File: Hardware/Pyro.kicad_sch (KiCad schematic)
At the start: 60 parts, among them J12 Conn_01x02_Male, J14 Conn_01x02_Male, J15 Conn_01x02_Male, Q7 BSZ025N04LS, Q8 BSZ025N04LS, Q9 BSZ025N04LS, U10 SiC438BED-T1-GE3, U11 782-TCMT1109, U12 INA219AxDCN, U15 782-TCMT1109, U9 782-TCMT1109

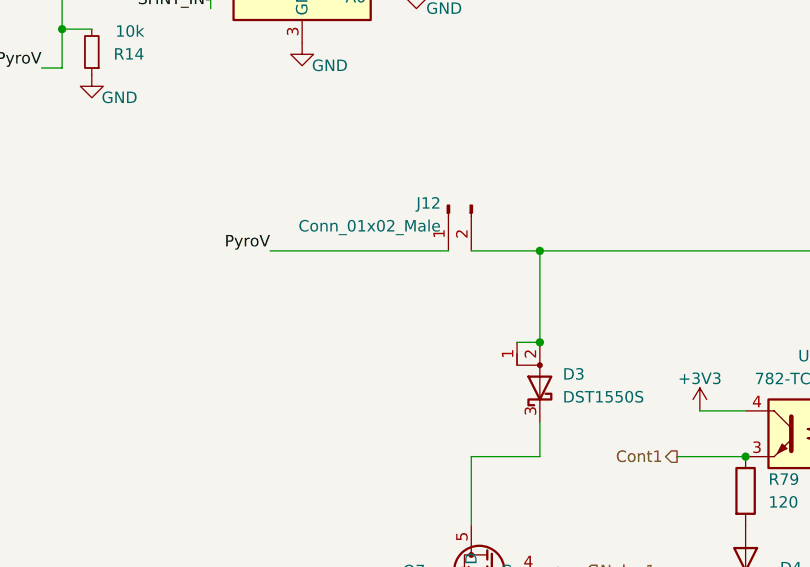
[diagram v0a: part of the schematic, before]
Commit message: Added flyback on pyro channel
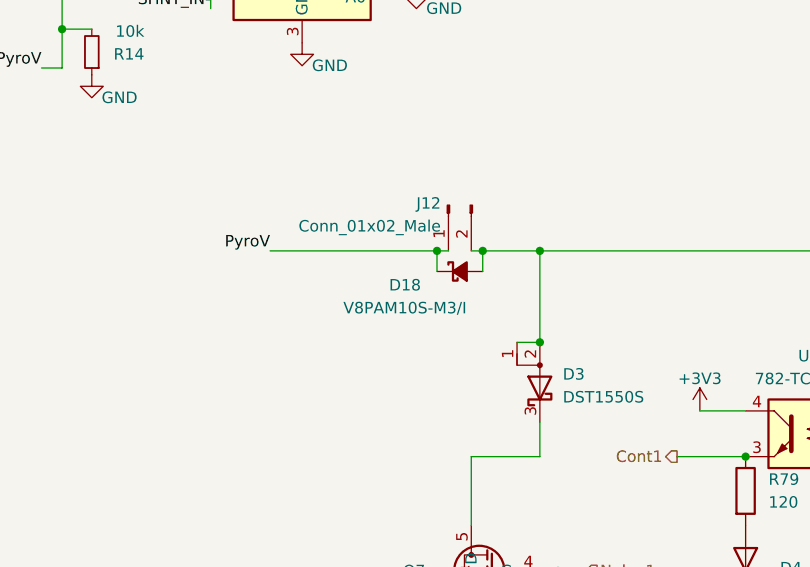
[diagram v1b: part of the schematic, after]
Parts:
- added D18: V8PAM10S-M3/I, iclr:V8PAM10SM3I, symbol Device:D_Schottky_Small_Filled
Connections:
- net PyroV: now also D18.1 (K)
- net at D3.1 (A), D3.2 (A), J12.2 (Pin_2)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: now also D18.2 (A)
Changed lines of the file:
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@@
 	)
 	(junction
+		(at 206.756 72.136)
+		(diameter 0)
+		(color 0 0 0 0)
+	)
+	(junction
 		(at 87.63 103.378)
 		(diameter 0)
@@
 		(color 0 0 0 0)
 	)
+	(junction
+		(at 211.836 72.136)
+		(diameter 0)
+		(color 0 0 0 0)
+	)
 	(no_connect
 		(at 42.672 51.054)
@@
 	(wire
 		(pts
+			(xy 206.756 72.136) (xy 208.026 72.136)
+		)
+		(stroke
+			(width 0)
+			(type default)
+		)
+	)
+	(wire
+		(pts
 			(xy 135.89 185.42) (xy 135.89 186.436)
 		)
@@
 	(wire
 		(pts
+			(xy 211.836 72.136) (xy 211.836 74.422)
+		)
+		(stroke
+			(width 0)
+			(type default)
+		)
+	)
+	(wire
+		(pts
 			(xy 40.64 132.08) (xy 41.91 132.08)
 		)
@@
 	(wire
 		(pts
+			(xy 206.756 72.136) (xy 206.756 74.422)
+		)
+		(stroke
+			(width 0)
+			(type default)
+		)
+	)
+	(wire
+		(pts
 			(xy 241.046 112.776) (xy 248.666 112.776)
 		)
@@
 	(wire
 		(pts
-			(xy 210.566 72.136) (xy 218.186 72.136)
+			(xy 210.566 72.136) (xy 211.836 72.136)
 		)
 		(stroke
@@
 	(wire
 		(pts
-			(xy 188.214 72.136) (xy 208.026 72.136)
+			(xy 188.214 72.136) (xy 206.756 72.136)
 		)
 		(stroke
@@
 	(wire
 		(pts
+			(xy 211.836 72.136) (xy 218.186 72.136)
+		)
+		(stroke
+			(width 0)
+			(type default)
+		)
+	)
+	(wire
+		(pts
 			(xy 191.77 21.082) (xy 195.58 21.082)
 		)
@@
 					(unit 1)
 				)
+			)
+		)
+	)
+	(symbol
+		(lib_id "Device:D_Schottky_Small_Filled")
+		(at 209.296 74.422 0)
+		(unit 1)
+		(exclude_from_sim no)
+		(in_bom yes)
+		(on_board yes)
+		(dnp no)
+		(property "Reference" "D18"
+			(at 203.2 75.946 0)
+			(effects
+				(font
+					(size 1.27 1.27)
+				)
+			)
+		)
+		(property "Value" "V8PAM10S-M3/I"
+			(at 203.2 78.486 0)
+			(effects
+				(font
+					(size 1.27 1.27)
+				)
+			)
+		)
+		(property "Footprint" "iclr:V8PAM10SM3I"
+			(at 209.296 74.422 90)
+			(effects
+				(font
+					(size 1.27 1.27)
+				)
+				(hide yes)
+			)
+		)
+		(property "Datasheet" "~"
+			(at 209.296 74.422 90)
+			(effects
+				(font
+					(size 1.27 1.27)
+				)
+				(hide yes)
+			)
+		)
+		(property "Description" "Schottky diode, small symbol, filled shape"
+			(at 209.296 74.422 0)
+			(effects
+				(font
+					(size 1.27 1.27)
+				)
+				(hide yes)
+			)
+		)
+		(pin "1"
+		)
+		(pin "2"
+		)
+		(instances
+			(project "Ricardo-Stark"
+				(path "/7db990e4-92e1-4f99-b4d2-435bbec1ba83/3c6662b6-8783-49dc-b944-3dc2b3e30a07"
+					(reference "D18")
+					(unit 1)
+				)

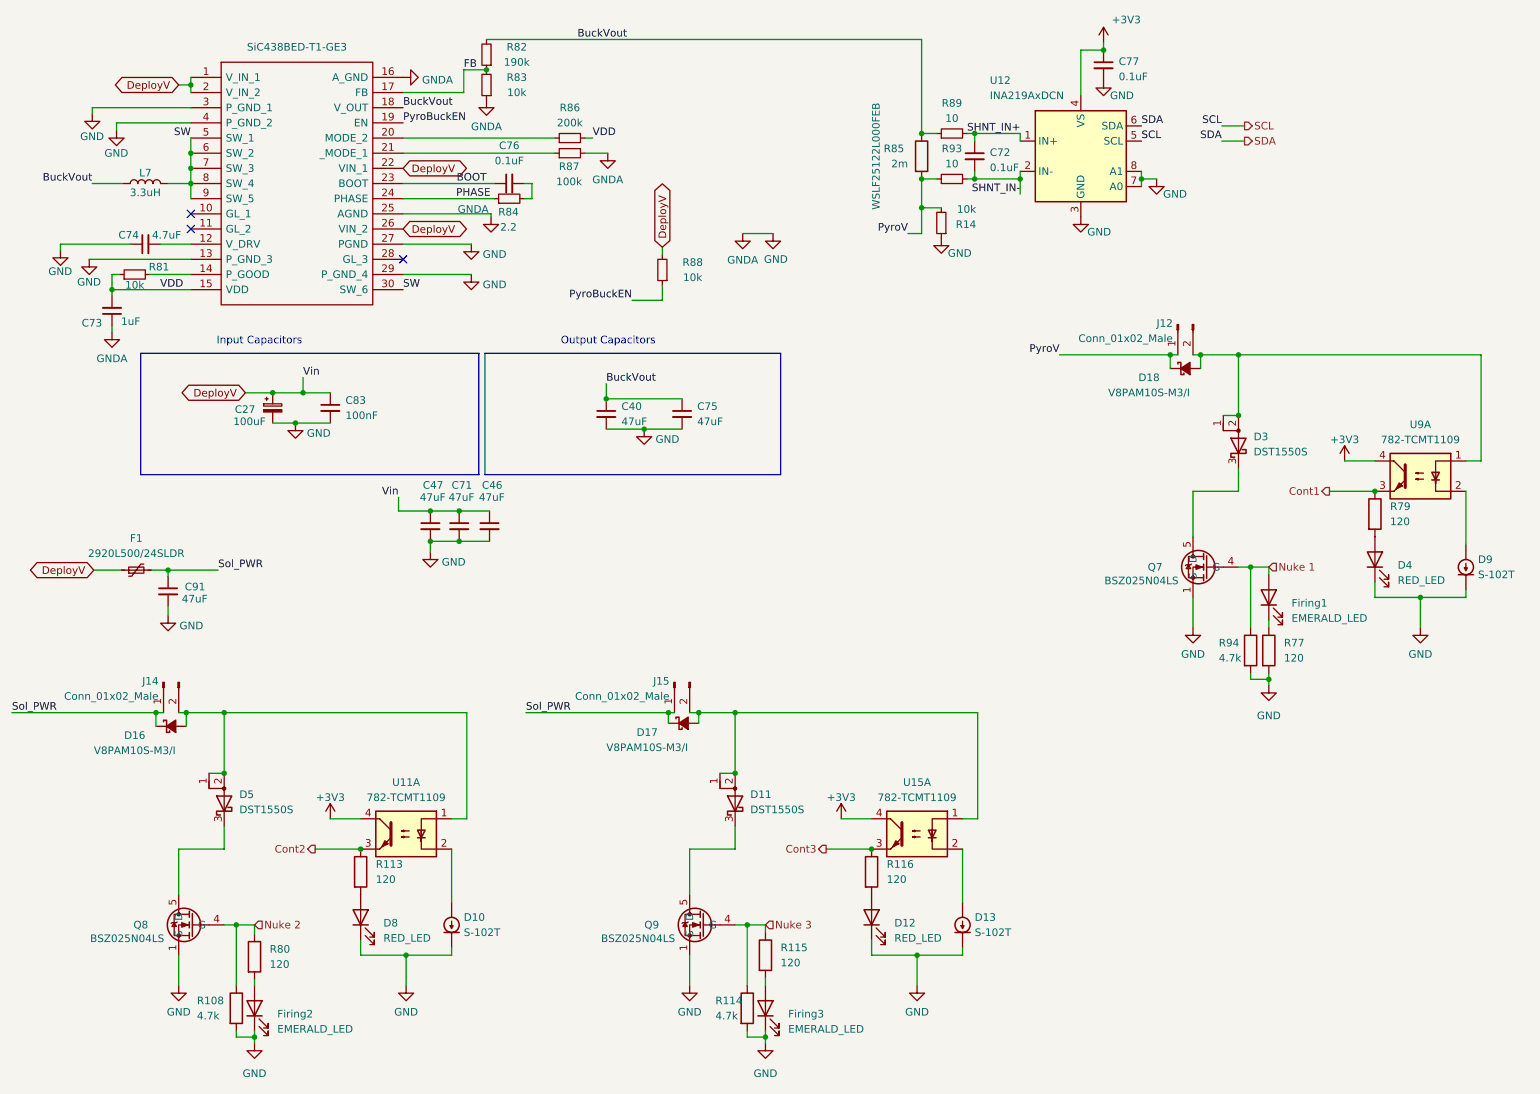
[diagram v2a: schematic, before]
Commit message: schematic reformatting and bom consolidation
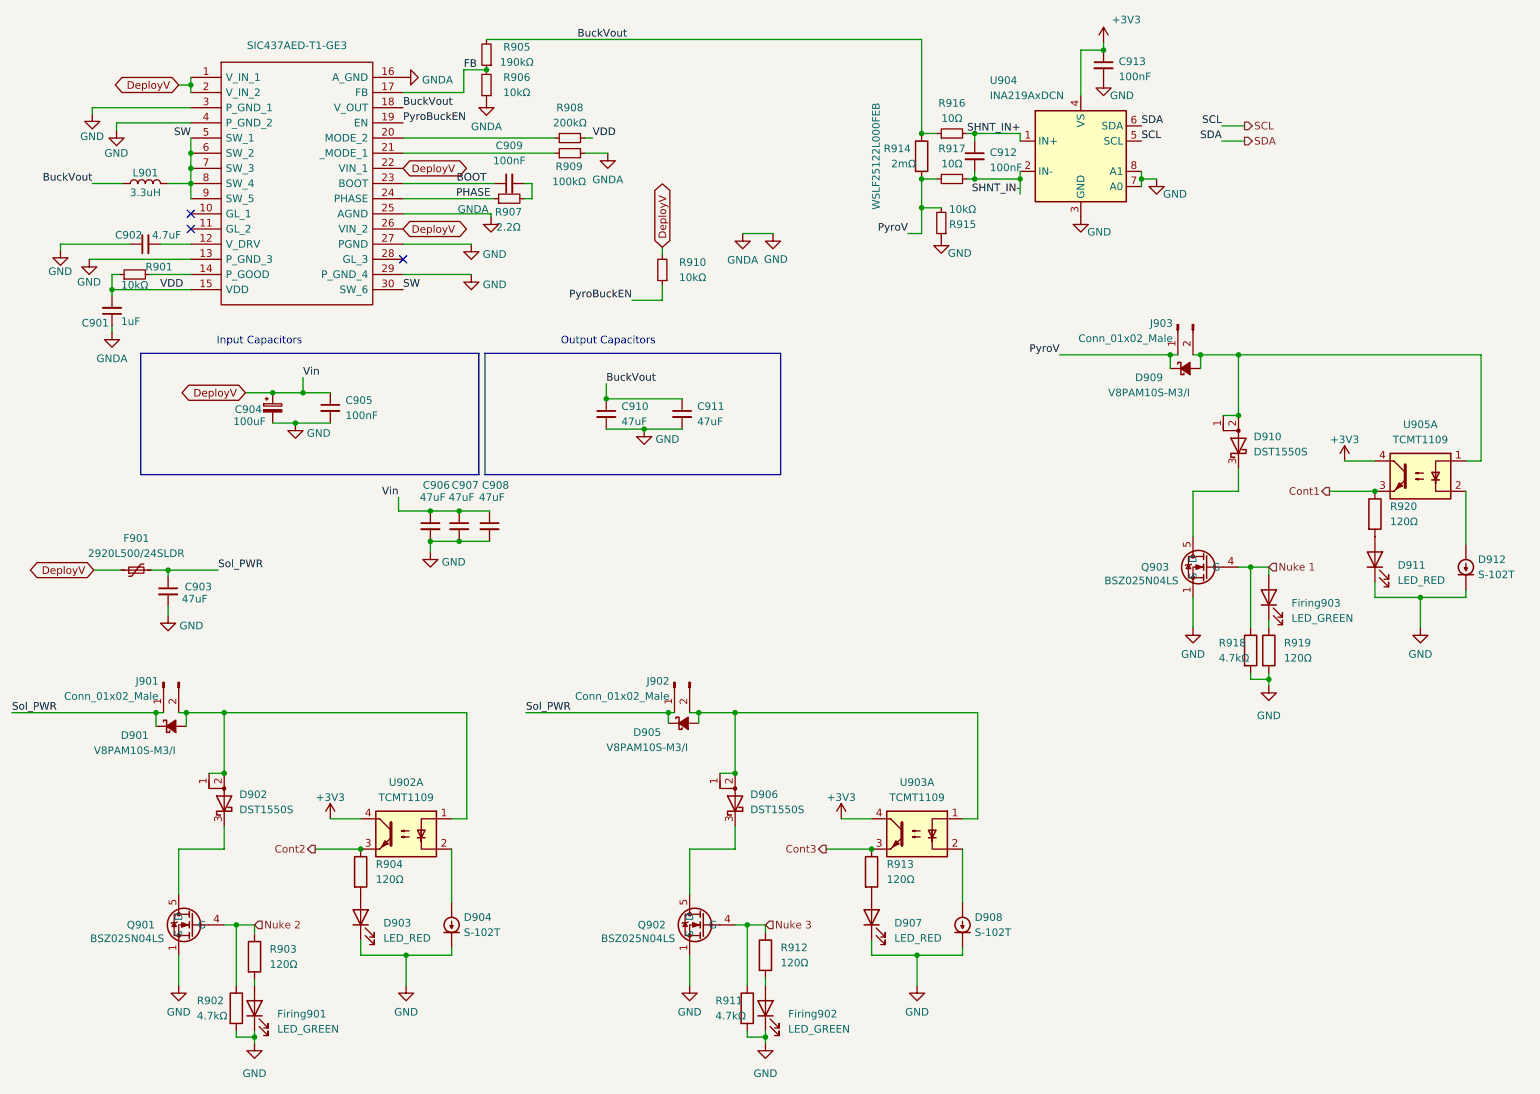
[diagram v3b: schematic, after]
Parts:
- C909: renamed from C76; value 0.1uF -> 100nF
- C912: renamed from C72; value 0.1uF -> 100nF
- C913: renamed from C77; value 0.1uF -> 100nF
- D903: renamed from D8; value RED_LED -> LED_RED
- D907: renamed from D12; value RED_LED -> LED_RED
- D911: renamed from D4; value RED_LED -> LED_RED
- Firing901: renamed from Firing2; value EMERALD_LED -> LED_GREEN
- Firing902: renamed from Firing3; value EMERALD_LED -> LED_GREEN
- Firing903: renamed from Firing1; value EMERALD_LED -> LED_GREEN
- R901: renamed from R81; value 10k -> 10kΩ
- R902: renamed from R108; value 4.7k -> 4.7kΩ
- R903: renamed from R80; value 120 -> 120Ω
- R904: renamed from R113; value 120 -> 120Ω
- R905: renamed from R82; value 190k -> 190kΩ
- R906: renamed from R83; value 10k -> 10kΩ
- R907: renamed from R84; value 2.2 -> 2.2Ω
- R908: renamed from R86; value 200k -> 200kΩ
- R909: renamed from R87; value 100k -> 100kΩ
- R910: renamed from R88; value 10k -> 10kΩ
- R911: renamed from R114; value 4.7k -> 4.7kΩ
- R912: renamed from R115; value 120 -> 120Ω
- R913: renamed from R116; value 120 -> 120Ω
- R914: renamed from R85; value 2m -> 2mΩ
- R915: renamed from R14; value 10k -> 10kΩ
- R916: renamed from R89; value 10 -> 10Ω
- R917: renamed from R93; value 10 -> 10Ω
- R918: renamed from R94; value 4.7k -> 4.7kΩ
- R919: renamed from R77; value 120 -> 120Ω
- R920: renamed from R79; value 120 -> 120Ω
- U901: renamed from U10; value SiC438BED-T1-GE3 -> SIC437AED-T1-GE3
- U902: renamed from U11; value 782-TCMT1109 -> TCMT1109
- U903: renamed from U15; value 782-TCMT1109 -> TCMT1109
- U905: renamed from U9; value 782-TCMT1109 -> TCMT1109
- renumbered C73 to C901, C74 to C902, C91 to C903, C27 to C904, C83 to C905, C47 to C906, C71 to C907, C46 to C908, C40 to C910, C75 to C911, D16 to D901, D5 to D902, D10 to D904, D17 to D905, D11 to D906, D13 to D908, D18 to D909, D3 to D910, D9 to D912, F1 to F901, J14 to J901, J15 to J902, J12 to J903, L7 to L901, Q8 to Q901, Q9 to Q902, Q7 to Q903, U12 to U904

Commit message: changed fp
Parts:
- U902, U903, U905: footprint iclr:TCMT1109-4N -> Package_SO:SOP-4_4.4x2.6mm_P1.27mm
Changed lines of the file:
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@@
 			)
 		)
-		(property "Footprint" "iclr:TCMT1109-4N"
+		(property "Footprint" "Package_SO:SOP-4_4.4x2.6mm_P1.27mm"
 			(at 83.82 157.48 0)
 			(effects
@@
 			)
 		)
-		(property "Footprint" "iclr:TCMT1109-4N"
+		(property "Footprint" "Package_SO:SOP-4_4.4x2.6mm_P1.27mm"
 			(at 169.418 157.48 0)
 			(effects
@@
 			)
 		)
-		(property "Footprint" "iclr:TCMT1109-4N"
+		(property "Footprint" "Package_SO:SOP-4_4.4x2.6mm_P1.27mm"
 			(at 253.746 97.536 0)
 			(effects
